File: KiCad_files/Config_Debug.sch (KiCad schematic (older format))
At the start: 58 parts, among them J3 Conn_01x06, J4 USB_C_Receptacle, J8 Conn_01x02, J9 Conn_01x02, SW1 SW_Push, U1 XC7A35T_CSG325, U10 W25Q128JV, U6 FT2232HL, U7 93LCxxC, U8 SiT8209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

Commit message: Added 5V supply for HDMI.
Added jumper for USB-C power
TODO:
Add more jumpers (EMCCLK and Config)
Add lots of test points
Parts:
- added J12: Conn_01x03, symbol Connector_Generic:Conn_01x03
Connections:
- net USB_VBUS_1: now also J12.1 (Pin_1); no longer J4.A4 (VBUS), J4.A9 (VBUS), J4.B4 (VBUS), J4.B9 (VBUS)
- new net: J12.2 (Pin_2), J4.A4 (VBUS), J4.A9 (VBUS), J4.B4 (VBUS), J4.B9 (VBUS)
- new net VCC5V0: J12.3 (Pin_3)
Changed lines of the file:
@@
 NoConn ~ 1800 5350
 NoConn ~ 1800 5250
-Text GLabel 2000 5050 2    60   Input ~ 0
+Text GLabel 2000 4800 2    60   Input ~ 0
 USB_VBUS_1
 Text GLabel 2000 5550 2    60   Input ~ 0
@@
 Wire Wire Line
 	1800 5050 2000 5050
+Text GLabel 2000 5300 2    60   Input ~ 0
+VCC5V0
+$Comp
+L Connector_Generic:Conn_01x03 J12
+U 1 1 5C7E7D5A
+P 2200 5050
+F 0 "J12" H 2280 5046 50  0000 L CNN
+F 1 "Conn_01x03" H 2280 5001 50  0001 L CNN
+F 2 "" H 2200 5050 50  0001 C CNN
+F 3 "~" H 2200 5050 50  0001 C CNN
+	1    2200 5050
+	1    0    0    -1
+$EndComp
+Wire Wire Line
+	2000 5150 1950 5150
+Wire Wire Line
+	1950 5150 1950 5300
+Wire Wire Line
+	1950 5300 2000 5300
+Wire Wire Line
+	2000 4950 1950 4950
+Wire Wire Line
+	1950 4950 1950 4800
+Wire Wire Line
+	1950 4800 2000 4800
 $EndSCHEMATC

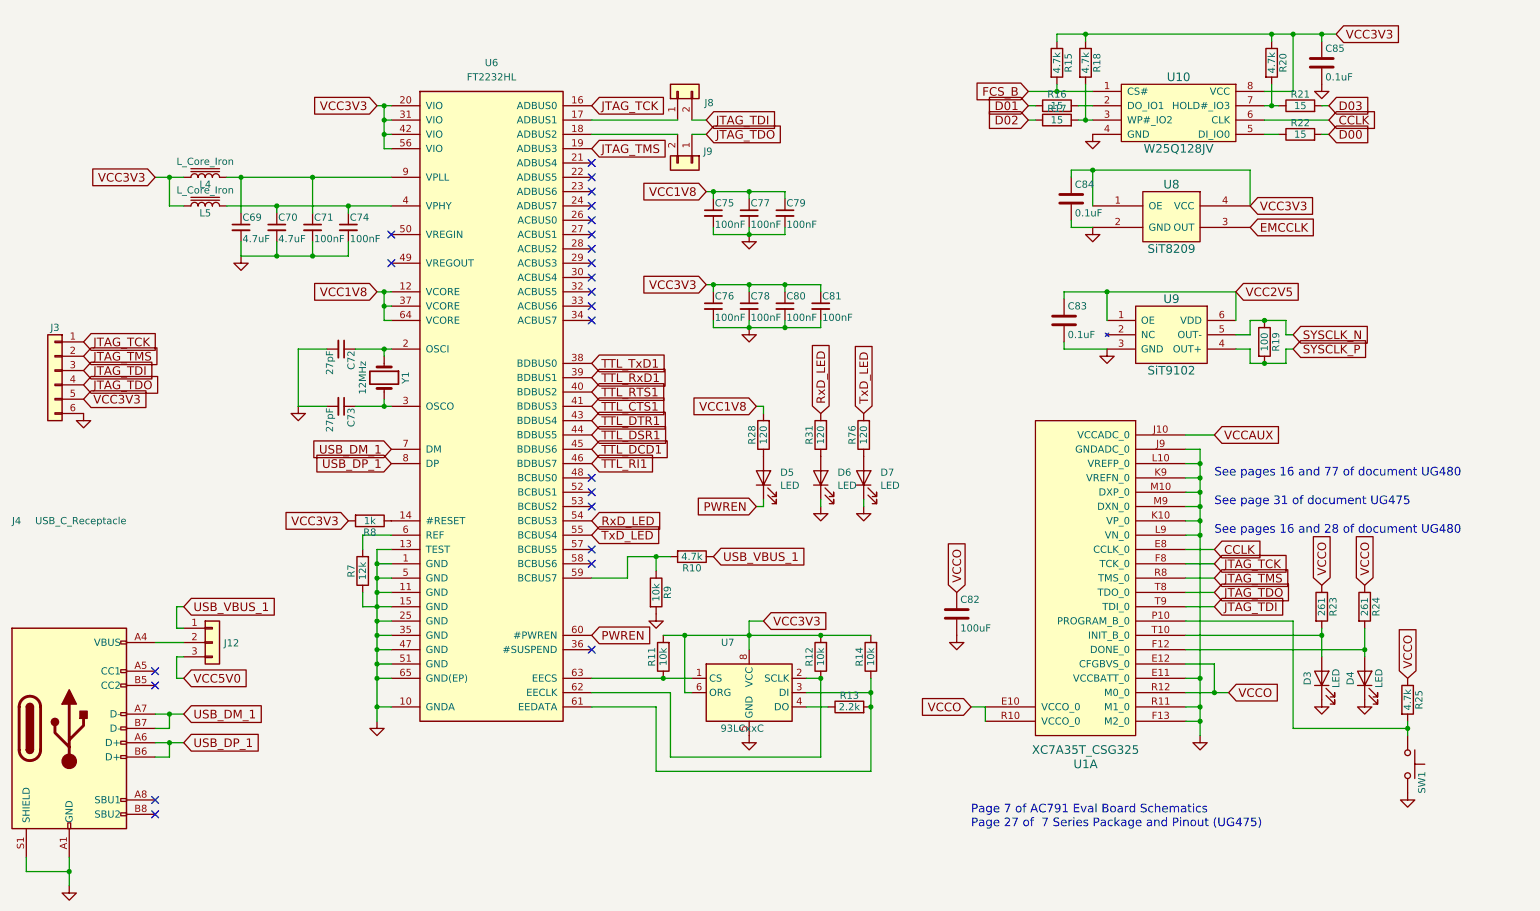
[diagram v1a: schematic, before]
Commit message: Added more caps and jumpers for EMCCLK & Config
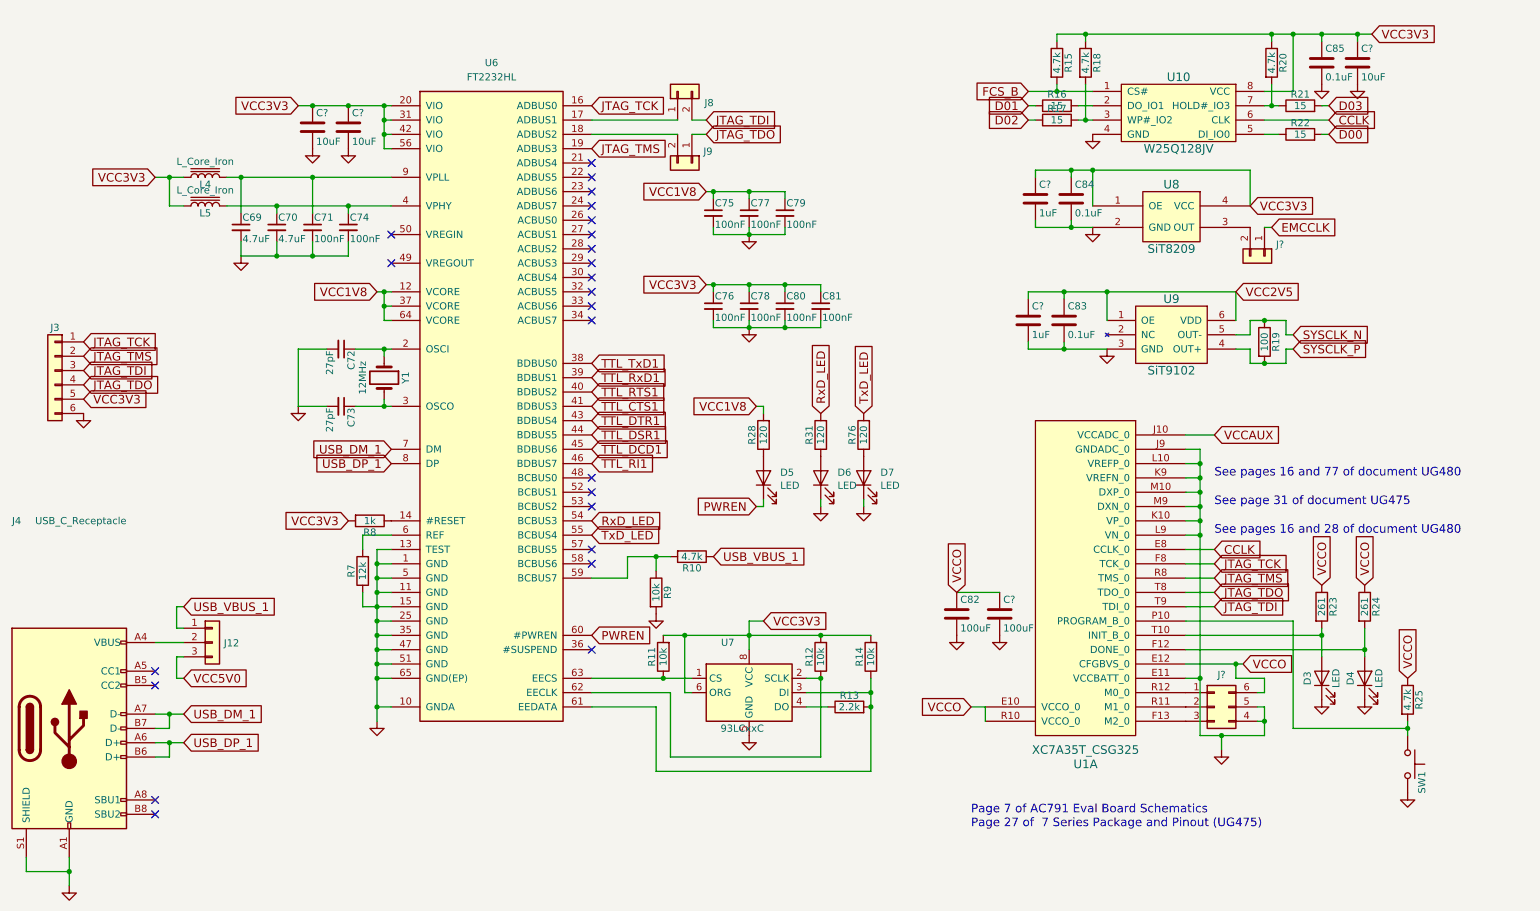
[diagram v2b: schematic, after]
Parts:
- added C?: 100uF, symbol Device:C
- added C? (x3): 10uF, symbol Device:C
- added C? (x2): 1uF, symbol Device:C
- added J?: Conn_01x02, symbol Connector_Generic:Conn_01x02
- added J?: Conn_02x03_Counter_Clockwise, symbol Connector_Generic:Conn_02x03_Counter_Clockwise
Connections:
- net EMCCLK: now also J?.1 (Pin_1); no longer U8.3 (OUT)
- net GND: now also C?.2, C?.2, C?.2, C?.2, C?.2, C?.2, J?.4 (Pin_4), J?.5 (Pin_5); no longer U1.F13 (M2_0), U1.R11 (M1_0)
- net VCC2V5: now also C?.1
- net VCC3V3: now also C?.1, C?.1, C?.1, C?.1
- net VCCO: now also C?.1, J?.6 (Pin_6); no longer U1.R12 (M0_0)
- new net: J?.3 (Pin_3), U1.F13 (M2_0)
- new net: J?.2 (Pin_2), U1.R11 (M1_0)
- new net: J?.1 (Pin_1), U1.R12 (M0_0)
- new net: J?.2 (Pin_2), U8.3 (OUT)
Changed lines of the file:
@@
 L power:GND #PWR086
 U 1 1 5C09142B
-P 9100 5700
-F 0 "#PWR086" H 9100 5450 50  0001 C CNN
-F 1 "GND" H 9100 5550 50  0001 C CNN
-F 2 "" H 9100 5700 50  0001 C CNN
-F 3 "" H 9100 5700 50  0001 C CNN
-	1    9100 5700
+P 9250 5800
+F 0 "#PWR086" H 9250 5550 50  0001 C CNN
+F 1 "GND" H 9250 5650 50  0001 C CNN
+F 2 "" H 9250 5800 50  0001 C CNN
+F 3 "" H 9250 5800 50  0001 C CNN
+	1    9250 5800
 	1    0    0    -1
 $EndComp
@@
 Text Notes 9200 4100 0    60   ~ 0
 See page 31 of document UG475
-Text GLabel 9300 5400 2    60   Input ~ 0
+Text GLabel 9400 5200 2    60   Input ~ 0
 VCCO
 $Comp
@@
 	1    0    0    -1
 $EndComp
-Text GLabel 10050 800  2    60   Input ~ 0
+Text GLabel 10300 800  2    60   Input ~ 0
 VCC3V3
 $Comp
@@
 Wire Wire Line
 	9000 3700 9100 3700
-Connection ~ 9100 5300
 Wire Wire Line
 	9000 4500 9200 4500
@@
 	9000 4300 9100 4300
 Connection ~ 9100 4300
-Wire Wire Line
-	9000 5500 9100 5500
-Connection ~ 9100 5500
-Wire Wire Line
-	9000 5600 9100 5600
-Connection ~ 9100 5600
-Wire Wire Line
-	9000 5400 9200 5400
-Wire Wire Line
-	9000 5200 9200 5200
-Wire Wire Line
-	9200 5200 9200 5400
-Connection ~ 9200 5400
 Wire Wire Line
 	9950 4950 9950 5000
@@
 	8100 1150 8100 1200
 Connection ~ 8100 1200
-Text GLabel 9450 2150 2    60   Input ~ 0
+Text GLabel 9600 2150 2    60   Input ~ 0
 EMCCLK
 Text GLabel 9450 2000 2    60   Input ~ 0
@@
 	1    0    0    -1
 $EndComp
-Text GLabel 3350 1300 0    60   Input ~ 0
+Text GLabel 2800 1300 0    60   Input ~ 0
 VCC3V3
 Text GLabel 3350 2600 0    60   Input ~ 0
@@
 Connection ~ 3350 5500
 Wire Wire Line
-	3350 1300 3400 1300
-Wire Wire Line
 	3400 1300 3400 1400
 Wire Wire Line
@@
 $EndComp
 Wire Wire Line
-	9100 5300 9100 5500
-Wire Wire Line
 	9100 3800 9100 3900
 Wire Wire Line
@@
 	9100 4300 9100 5300
 Wire Wire Line
-	9100 5500 9100 5600
-Wire Wire Line
-	9100 5600 9100 5700
-Wire Wire Line
-	9200 5400 9300 5400
+	9250 5700 9250 5800
 Wire Wire Line
 	9950 5000 9950 5150
@@
 Wire Wire Line
 	9600 800  9750 800
-Wire Wire Line
-	9950 800  10050 800
 Wire Wire Line
 	8300 800  9600 800
@@
 Wire Wire Line
 	1950 4800 2000 4800
+$Comp
+L Device:C C?
+U 1 1 5C7A8FC9
+P 7700 4850
+AR Path="/5C064F83/5C7A8FC9" Ref="C?"  Part="1"
+AR Path="/5C0630AC/5C7A8FC9" Ref="C?"  Part="1"
+F 0 "C?" H 7725 4950 50  0000 L CNN
+F 1 "100uF" H 7725 4750 50  0000 L CNN
+F 2 "" H 7738 4700 50  0001 C CNN
+F 3 "" H 7700 4850 50  0001 C CNN
+	1    7700 4850
+	1    0    0    -1
+$EndComp
+$Comp
+L power:GND #PWR?
+U 1 1 5C7A8FD0
+P 7700 5000
+AR Path="/5C064F83/5C7A8FD0" Ref="#PWR?"  Part="1"
+AR Path="/5C0630AC/5C7A8FD0" Ref="#PWR?"  Part="1"
+F 0 "#PWR?" H 7700 4750 50  0001 C CNN
+F 1 "GND" H 7700 4850 50  0001 C CNN
+F 2 "" H 7700 5000 50  0001 C CNN
+F 3 "" H 7700 5000 50  0001 C CNN
+	1    7700 5000
+	1    0    0    -1
+$EndComp
+Wire Wire Line
+	7400 4700 7700 4700
+$Comp
+L Device:C C?
+U 1 1 5C7BFE87
+P 10200 1000
+F 0 "C?" H 10225 1100 50  0000 L CNN
+F 1 "10uF" H 10225 900 50  0000 L CNN
+F 2 "" H 10238 850 50  0001 C CNN
+F 3 "" H 10200 1000 50  0001 C CNN
+	1    10200 1000
+	1    0    0    -1
+$EndComp
+$Comp
+L power:GND #PWR?
+U 1 1 5C7BFE8E
+P 10200 1150
+F 0 "#PWR?" H 10200 900 50  0001 C CNN
+F 1 "GND" H 10200 1000 50  0001 C CNN
+F 2 "" H 10200 1150 50  0001 C CNN
+F 3 "" H 10200 1150 50  0001 C CNN
+	1    10200 1150
+	1    0    0    -1
+$EndComp
+Wire Wire Line
+	10200 850  10200 800
+Wire Wire Line
+	9950 800  10200 800
+Connection ~ 10200 800
+Wire Wire Line
+	10200 800  10300 800
+$Comp
+L Device:C C?
+U 1 1 5C7EA238
+P 7900 2800
+F 0 "C?" H 7925 2900 50  0000 L CNN
+F 1 "1uF" H 7925 2700 50  0000 L CNN
+F 2 "" H 7938 2650 50  0001 C CNN
+F 3 "" H 7900 2800 50  0001 C CNN
+	1    7900 2800
+	1    0    0    -1
+$EndComp
+Wire Wire Line
+	7900 2950 7900 3000
+Wire Wire Line
+	7900 3000 8150 3000
+Connection ~ 8150 3000
+Wire Wire Line
+	8150 2600 7900 2600
+Wire Wire Line
+	7900 2600 7900 2650
+Connection ~ 8150 2600
+$Comp
+L Device:C C?
+U 1 1 5C81375F
+P 7950 1950
+F 0 "C?" H 7975 2050 50  0000 L CNN
+F 1 "1uF" H 7975 1850 50  0000 L CNN
+F 2 "" H 7988 1800 50  0001 C CNN
+F 3 "" H 7950 1950 50  0001 C CNN
+	1    7950 1950
+	1    0    0    -1
+$EndComp
+Wire Wire Line
+	7950 1800 7950 1750
+Wire Wire Line
+	7950 1750 8200 1750
+Connection ~ 8200 1750
+Wire Wire Line
+	8200 2150 7950 2150
+Wire Wire Line
+	7950 2150 7950 2100
+Connection ~ 8200 2150
+$Comp
+L Device:C C?
+U 1 1 5C83BC44
+P 3150 1450
+F 0 "C?" H 3175 1550 50  0000 L CNN
+F 1 "10uF" H 3175 1350 50  0000 L CNN
+F 2 "" H 3188 1300 50  0001 C CNN
+F 3 "" H 3150 1450 50  0001 C CNN
+	1    3150 1450
+	1    0    0    -1
+$EndComp
+$Comp
+L power:GND #PWR?
+U 1 1 5C83BC4B
+P 3150 1600
+F 0 "#PWR?" H 3150 1350 50  0001 C CNN
+F 1 "GND" H 3150 1450 50  0001 C CNN
+F 2 "" H 3150 1600 50  0001 C CNN
+F 3 "" H 3150 1600 50  0001 C CNN
+	1    3150 1600
+	1    0    0    -1
+$EndComp
+$Comp
+L Device:C C?
+U 1 1 5C84FF3B
+P 2900 1450
+F 0 "C?" H 2925 1550 50  0000 L CNN
+F 1 "10uF" H 2925 1350 50  0000 L CNN
+F 2 "" H 2938 1300 50  0001 C CNN
+F 3 "" H 2900 1450 50  0001 C CNN
+	1    2900 1450
+	1    0    0    -1
+$EndComp
+$Comp
+L power:GND #PWR?
+U 1 1 5C84FF42
+P 2900 1600
+F 0 "#PWR?" H 2900 1350 50  0001 C CNN
+F 1 "GND" H 2900 1450 50  0001 C CNN
+F 2 "" H 2900 1600 50  0001 C CNN
+F 3 "" H 2900 1600 50  0001 C CNN
+	1    2900 1600
+	1    0    0    -1
+$EndComp
+Wire Wire Line
+	2800 1300 2900 1300
+Connection ~ 2900 1300
+Wire Wire Line
+	2900 1300 3150 1300
+Connection ~ 3150 1300
+Wire Wire Line
+	3150 1300 3400 1300
+$Comp
+L Connector_Generic:Conn_01x02 J?
+U 1 1 5C87AC76
+P 9550 2350
+F 0 "J?" V 9469 2430 50  0000 L CNN
+F 1 "Conn_01x02" V 9514 2430 50  0001 L CNN
+F 2 "" H 9550 2350 50  0001 C CNN
+F 3 "~" H 9550 2350 50  0001 C CNN
+	1    9550 2350
+	0    1    1    0
+$EndComp
+Wire Wire Line
+	9600 2150 9550 2150
+$Comp
+L Connector_Generic:Conn_02x03_Counter_Clockwise J?
+U 1 1 5C8D400A
+P 9200 5500
+F 0 "J?" H 9250 5725 50  0000 C CNN
+F 1 "Conn_02x03_Counter_Clockwise" H 9250 5726 50  0001 C CNN
+F 2 "" H 9200 5500 50  0001 C CNN
+F 3 "~" H 9200 5500 50  0001 C CNN
+	1    9200 5500
+	1    0    0    -1
+$EndComp
+Wire Wire Line
+	9000 5200 9350 5200
+Wire Wire Line
+	9350 5200 9350 5300
+Wire Wire Line
+	9350 5300 9550 5300
+Wire Wire Line
+	9550 5300 9550 5400
+Wire Wire Line
+	9550 5400 9500 5400
+Connection ~ 9350 5200
+Wire Wire Line
+	9350 5200 9400 5200
+Wire Wire Line
+	9500 5500 9550 5500
+Wire Wire Line
+	9550 5500 9550 5600
+Wire Wire Line
+	9550 5700 9250 5700
+Wire Wire Line
+	9500 5600 9550 5600
+Connection ~ 9550 5600
+Wire Wire Line
+	9550 5600 9550 5700
+Wire Wire Line
+	9100 5300 9100 5700
+Wire Wire Line
+	9100 5700 9250 5700
+Connection ~ 9100 5300
+Connection ~ 9250 5700
 $EndSCHEMATC

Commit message: More caps and added lots of test points
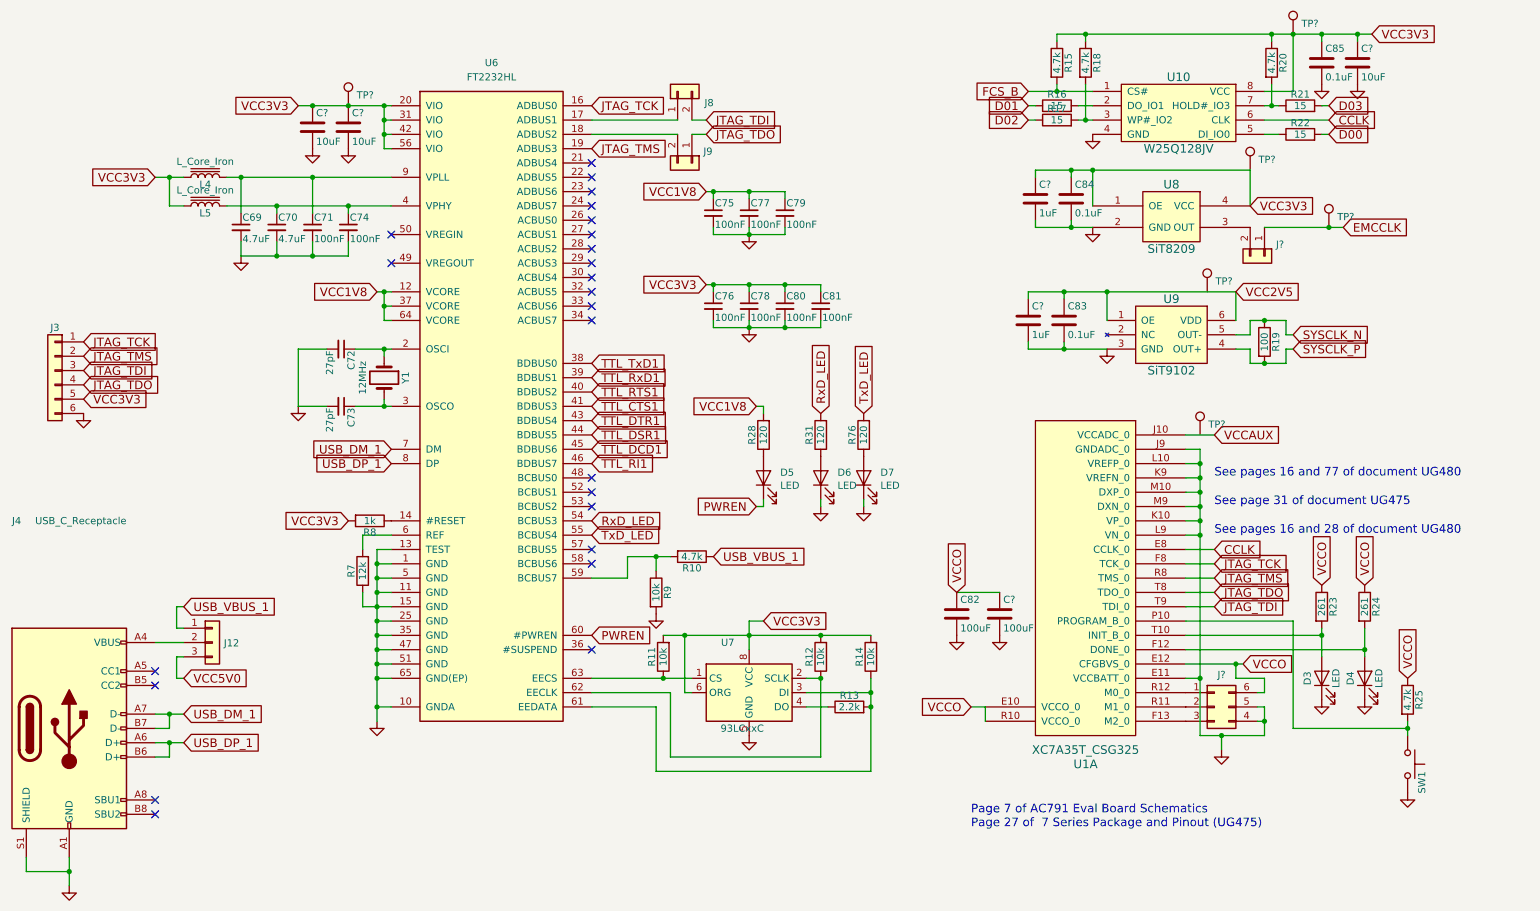
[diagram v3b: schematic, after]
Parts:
- added TP? (x6): TestPoint, symbol Connector:TestPoint
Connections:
- net EMCCLK: now also TP?.1
- net VCC3V3: now also TP?.1, TP?.1, TP?.1
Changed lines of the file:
@@
 	8100 1150 8100 1200
 Connection ~ 8100 1200
-Text GLabel 9600 2150 2    60   Input ~ 0
+Text GLabel 10100 2150 2    60   Input ~ 0
 EMCCLK
 Text GLabel 9450 2000 2    60   Input ~ 0
@@
 	0    1    1    0
 $EndComp
-Wire Wire Line
-	9600 2150 9550 2150
 $Comp
 L Connector_Generic:Conn_02x03_Counter_Clockwise J?
@@
 Connection ~ 9100 5300
 Connection ~ 9250 5700
+$Comp
+L Connector:TestPoint TP?
+U 1 1 5CDCFA60
+P 3150 1300
+AR Path="/5BFDDAF0/5CDCFA60" Ref="TP?"  Part="1"
+AR Path="/5C0630AC/5CDCFA60" Ref="TP?"  Part="1"
+F 0 "TP?" H 3208 1374 50  0000 L CNN
+F 1 "TestPoint" H 3208 1329 50  0001 L CNN
+F 2 "" H 3350 1300 50  0001 C CNN
+F 3 "~" H 3350 1300 50  0001 C CNN
+	1    3150 1300
+	1    0    0    -1
+$EndComp
+$Comp
+L Connector:TestPoint TP?
+U 1 1 5CDE48B6
+P 9100 3600
+AR Path="/5BFDDAF0/5CDE48B6" Ref="TP?"  Part="1"
+AR Path="/5C0630AC/5CDE48B6" Ref="TP?"  Part="1"
+F 0 "TP?" H 9158 3674 50  0000 L CNN
+F 1 "TestPoint" H 9158 3629 50  0001 L CNN
+F 2 "" H 9300 3600 50  0001 C CNN
+F 3 "~" H 9300 3600 50  0001 C CNN
+	1    9100 3600
+	1    0    0    -1
+$EndComp
+$Comp
+L Connector:TestPoint TP?
+U 1 1 5CDF99BD
+P 9750 800
+AR Path="/5BFDDAF0/5CDF99BD" Ref="TP?"  Part="1"
+AR Path="/5C0630AC/5CDF99BD" Ref="TP?"  Part="1"
+F 0 "TP?" H 9808 874 50  0000 L CNN
+F 1 "TestPoint" H 9808 829 50  0001 L CNN
+F 2 "" H 9950 800 50  0001 C CNN
+F 3 "~" H 9950 800 50  0001 C CNN
+	1    9750 800
+	1    0    0    -1
+$EndComp
+$Comp
+L Connector:TestPoint TP?
+U 1 1 5CE0E801
+P 9450 1750
+AR Path="/5BFDDAF0/5CE0E801" Ref="TP?"  Part="1"
+AR Path="/5C0630AC/5CE0E801" Ref="TP?"  Part="1"
+F 0 "TP?" H 9508 1824 50  0000 L CNN
+F 1 "TestPoint" H 9508 1779 50  0001 L CNN
+F 2 "" H 9650 1750 50  0001 C CNN
+F 3 "~" H 9650 1750 50  0001 C CNN
+	1    9450 1750
+	1    0    0    -1
+$EndComp
+$Comp
+L Connector:TestPoint TP?
+U 1 1 5CE384ED
+P 9150 2600
+AR Path="/5BFDDAF0/5CE384ED" Ref="TP?"  Part="1"
+AR Path="/5C0630AC/5CE384ED" Ref="TP?"  Part="1"
+F 0 "TP?" H 9208 2674 50  0000 L CNN
+F 1 "TestPoint" H 9208 2629 50  0001 L CNN
+F 2 "" H 9350 2600 50  0001 C CNN
+F 3 "~" H 9350 2600 50  0001 C CNN
+	1    9150 2600
+	1    0    0    -1
+$EndComp
+$Comp
+L Connector:TestPoint TP?
+U 1 1 5CE6965B
+P 10000 2150
+F 0 "TP?" H 10058 2224 50  0000 L CNN
+F 1 "TestPoint" H 10058 2179 50  0001 L CNN
+F 2 "" H 10200 2150 50  0001 C CNN
+F 3 "~" H 10200 2150 50  0001 C CNN
+	1    10000 2150
+	1    0    0    -1
+$EndComp
+Wire Wire Line
+	9550 2150 10000 2150
+Connection ~ 10000 2150
+Wire Wire Line
+	10000 2150 10100 2150
 $EndSCHEMATC
